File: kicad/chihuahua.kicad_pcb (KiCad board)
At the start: 2 copper layers, 97.8 x 72.4 mm, 41 parts, among them J1 CARTRIDGE, J2 VIAport, J3 IOx, J4 nanoLink, J5 STEP, J6 POWER, Q1 BC548, Q2 BC548, SW1 RESET, SW2 NMI, U1 65C02, U2 65C22, U3 62256, U4 74HC132, U5 74HC32, X1 1 MHz

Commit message: v1.3
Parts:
- removed C2: 0, Capacitor_THT:CP_Radial_D4.0mm_P1.50mm
- removed D2: 1N4148, Diode_THT:D_DO-35_SOD27_P2.54mm_Vertical_AnodeUp
- added Q3: BC548, Package_TO_SOT_THT:TO-92_Inline, F.Cu at (45.1, 79.5)
- R4: value 3K3 -> 680
- moved BZ1 7.48 mm to (40.5, 81.3), turned to 180 degrees
- moved R4 2.56 mm to (55.9, 94.0), turned to 90 degrees
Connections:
- BZ1 pad 1: /CB2 -> /BCB2
- BZ1 pad 2: /D_PB7 -> /BPB7
- C1 pad 2: /U_RST -> /RST
- J1 pad 3: (no net) -> unconnected-(J1-Pin_3-Pad3)
- J1 pad 5: (no net) -> unconnected-(J1-Pin_5-Pad5)
- J1 pad 6: (no net) -> unconnected-(J1-Pin_6-Pad6)
- J2 pad 16: (no net) -> unconnected-(J2-Pin_16-Pad16)
- J2 pad 18: (no net) -> unconnected-(J2-Pin_18-Pad18)
- J2 pad 20: (no net) -> unconnected-(J2-Pin_20-Pad20)
- J2 pad 22: (no net) -> unconnected-(J2-Pin_22-Pad22)
- J2 pad 23: (no net) -> unconnected-(J2-Pin_23-Pad23)
- J2 pad 24: (no net) -> unconnected-(J2-Pin_24-Pad24)
- J2 pad 26: (no net) -> unconnected-(J2-Pin_26-Pad26)
- J4 pad 4: (no net) -> unconnected-(J4-Pin_4-Pad4)
- R4 pad 1: /U_NMI -> /RST
- R4 pad 2: GND -> /U_RST
- SW2 pad 1: /U_NMI -> GND
- SW2 pad 2: +5V -> /~{NMI}
- U1 pad 35: (no net) -> unconnected-(U1-N.C.-Pad35)
- U1 pad 5: (no net) -> unconnected-(U1-~{ML}-Pad5)
- U4 pad 1: /U_NMI -> +5V
- U4 pad 2: /U_NMI -> +5V
- U4 pad 3: /~{NMI} -> unconnected-(U4-Pad3)
- U4 pad 4: /U_RST -> /RST
- U4 pad 5: /U_RST -> /RST
- U5 pad 1: /CB2 -> PB7
- U5 pad 2: /CB2 -> PB7
- U5 pad 3: /CB2 -> /BPB7
- U5 pad 4: /CB2 -> PB7
- U5 pad 5: /CB2 -> PB7
- U5 pad 6: /CB2 -> /BPB7
- U5 pad 8: PB7 -> /BPB7
- X1 pad 1: (no net) -> unconnected-(X1-EN-Pad1)
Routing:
- net /BPB7: track 0.00 -> 26.3 mm, vias 0 -> 1
- net /U_NMI: track 25.9 -> 0.00 mm
- net GND: track 285.0 -> 306.4 mm
- net /R~{W}: track 97.3 -> 114.0 mm, vias 3 -> 5
- net /RST: track 0.00 -> 15.1 mm
- net /~{NMI}: track 126.9 -> 137.3 mm
- net /~{WE}: track 85.1 -> 77.1 mm
- net /U_RST: track 50.7 -> 44.4 mm
- net PB7: track 38.0 -> 43.6 mm
- net /D_PB7: track 5.63 -> 0.00 mm
- net /BCB2: track 0.00 -> 4.95 mm
- net /SCLK: track 87.2 -> 85.4 mm, vias 2 -> 1
- net /ROM_~{CS}: track 93.4 -> 91.6 mm
- net /CB2: track 104.9 -> 103.3 mm, vias 2 -> 3
- net +5V: track 388.0 -> 387.1 mm, vias 6 -> 4
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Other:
- board text added: "+5 PD0 BA0 PD1 BA1 PD2 BA2 PD3 BA3 PD4 ~WR PD5 ~IO PD6 GND PD7"
- board text added: "CLK ~RST GND D3 D2 D4 D1 D5 D0 D6 A0 D7 A1 ~CS A2 A10 A3 ~OE A4 A11 A5 A9 A6 A8 A7 A13 A12 A14 ~WE +5 * +5* ~NMI ~IRQ"
- board text added: "Chihuahua PLUS v1.3 (2024·6)"
- board text added: "GND SSCL SSDA ~STB +5"
- board text added: "PD0 +5 PD1 BA0 PD2 BA1 PD3 BA2 PD4 BA3 PD5 R~W PD6 ~IOX PD7 GND"
- board text removed: "+5 PD0 BA0 PD1 BA1 PD2 BA2 PD3 BA3 PD4 /WR PD5 /IO PD6 GND PD7"
- board text removed: "/RST SCLK D3 GND D4 D2 D5 D1 D6 D0 D7 A0 /CS A1 A10 A2 /OE A3 A11 A4 A9 A5 A8 A6 A13 A7 A14 A12 +5 /WE +5* * /IRQ /NMI"
- board text removed: "Chihuahua PLUS v1.2 (2024·4)"
- board text removed: "GND SSCL SSDA ~{STB +5}"
- board text removed: "PD0 +5 PD1 BA0 PD2 BA1 PD3 BA2 PD4 BA3 PD5 R~{W PD6} ~{IOX PD7} GND"

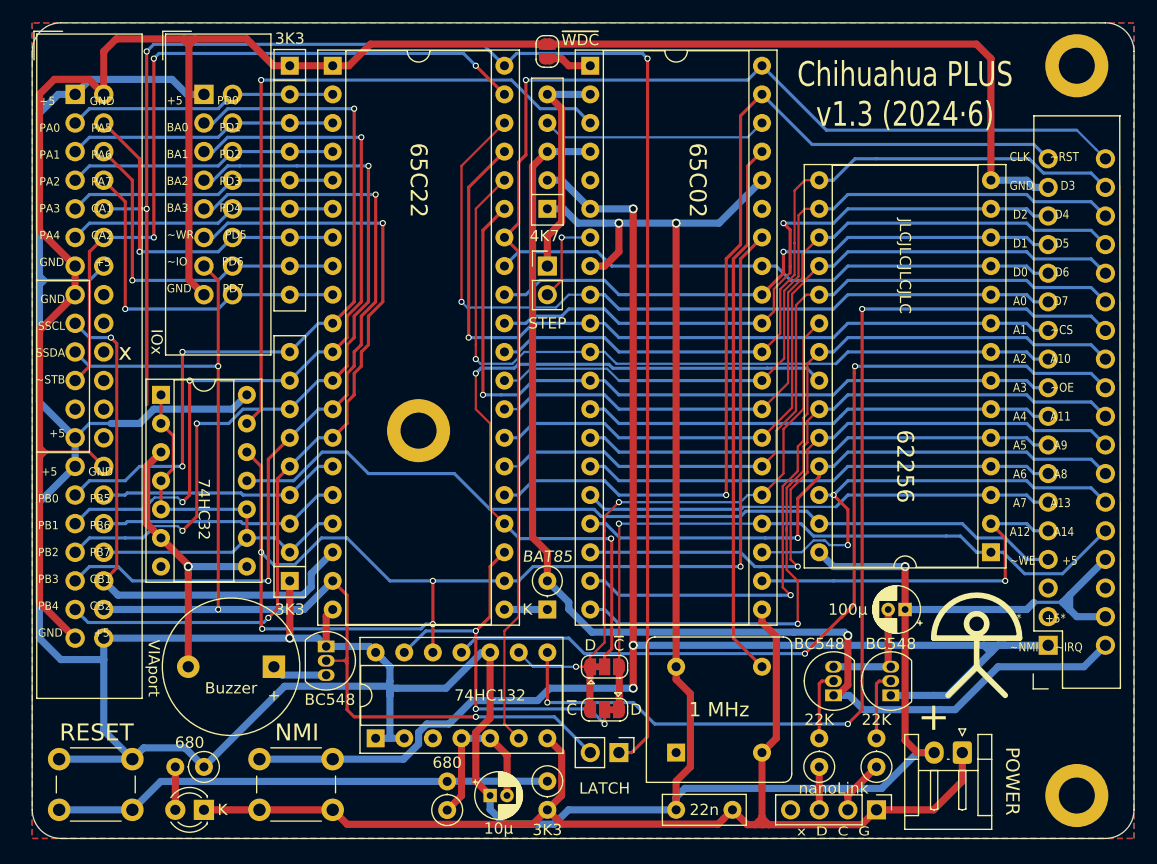
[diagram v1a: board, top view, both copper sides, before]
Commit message: improve power planes
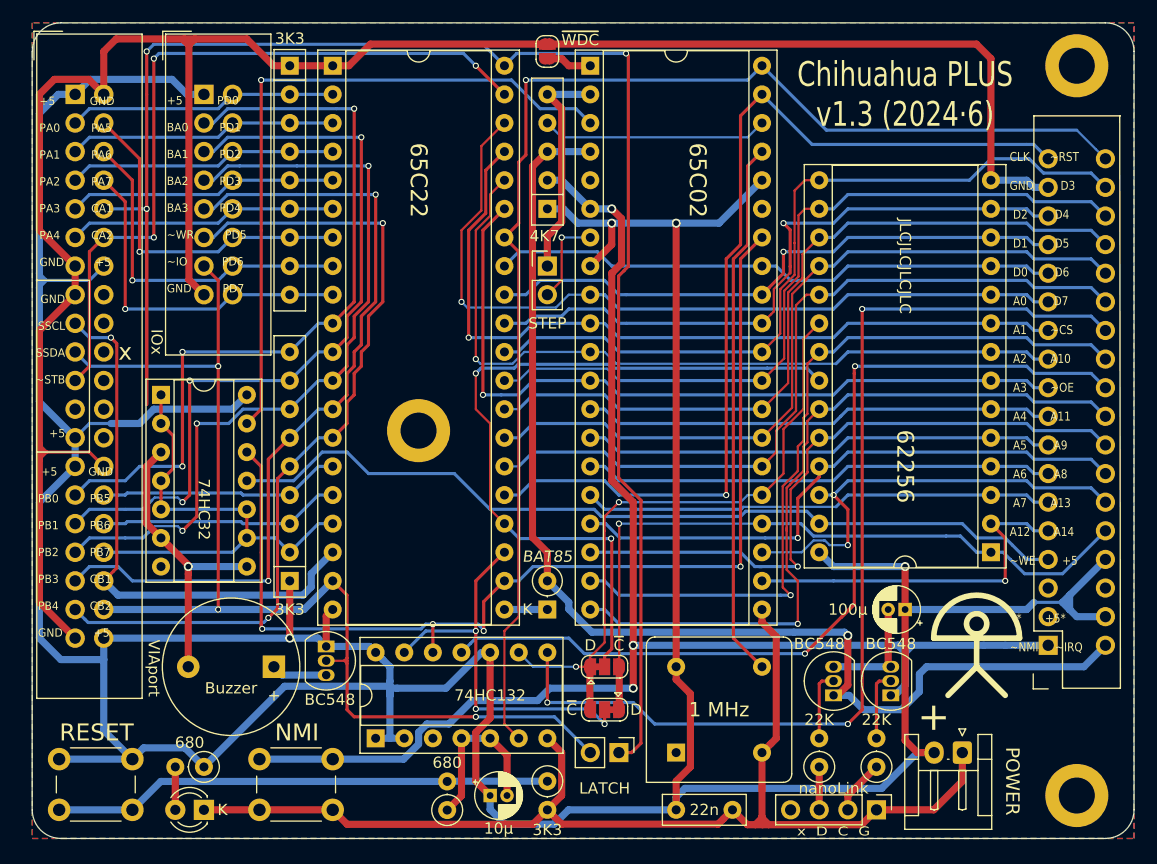
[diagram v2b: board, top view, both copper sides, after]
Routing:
- net /R~{W}: track 114.0 -> 95.6 mm, vias 5 -> 4
- net /~{NMI}: track 137.3 -> 131.0 mm
- net +5V: track 387.1 -> 386.1 mm
- net /~{IRQ}: track 105.1 -> 106.0 mm
- net /CA1: track 162.0 -> 161.3 mm
